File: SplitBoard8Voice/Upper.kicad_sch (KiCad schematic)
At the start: 18 parts, among them J801 A_UPPER, J802 B_UPPER, J803 C_UPPER, J804 D_UPPER, U801 40106, U802 CS5173

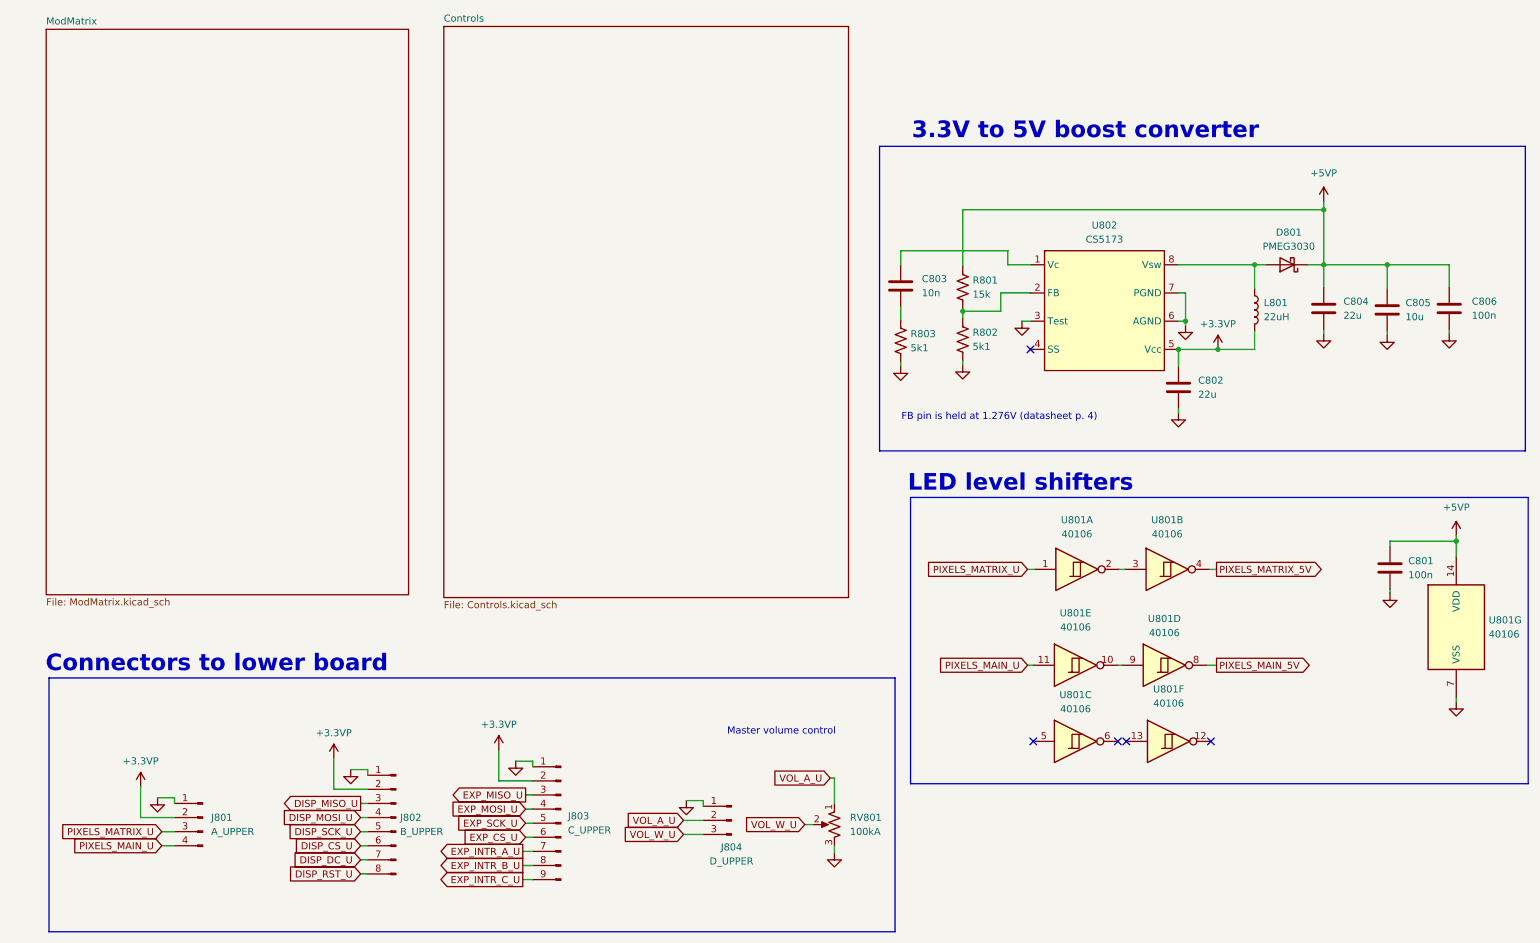
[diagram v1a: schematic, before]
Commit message: back to 3.3v LEDs
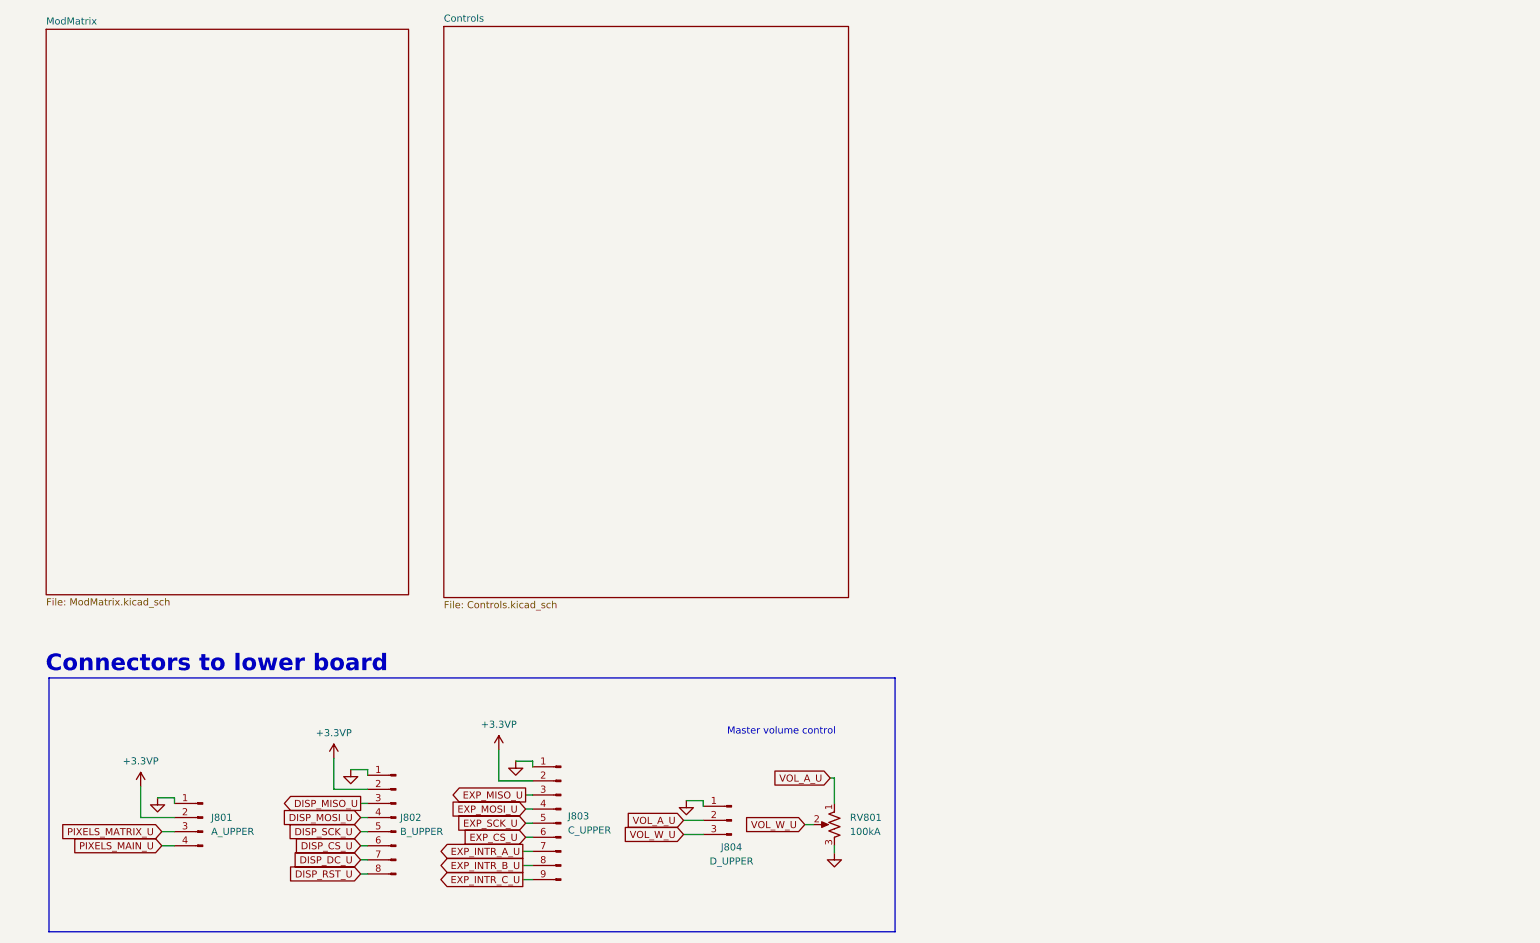
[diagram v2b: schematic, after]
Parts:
- removed C801, C806: 100n, Capacitor_SMD:C_0805_2012Metric, symbol Device:C
- removed C802, C804: 22u, Capacitor_SMD:C_0805_2012Metric, symbol Device:C
- removed C803: 10n, Capacitor_SMD:C_0805_2012Metric, symbol Device:C
- removed C805: 10u, Capacitor_SMD:C_0805_2012Metric, symbol Device:C
- removed D801: PMEG3030, Diode_SMD:D_SOD-123, symbol Device:D_Schottky
- removed L801: 22uH, Inductor_SMD:L_Changjiang_FNR4010S, symbol Device:L
- removed R801: 15k, Resistor_SMD:R_0805_2012Metric, symbol Device:R_US
- removed R802, R803: 5k1, Resistor_SMD:R_0805_2012Metric, symbol Device:R_US
- removed U801: 40106, Package_SO:SOIC-14_3.9x8.7mm_P1.27mm, symbol 4xxx:40106
- removed U802: CS5173, Package_SO:SOIC-8_3.9x4.9mm_P1.27mm, symbol cs5173:CS5173
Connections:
- no-connect marks 5 -> 0
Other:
- note removed: "3.3V to 5V boost converter"
- note removed: "FB pin is held at 1.276V (datasheet p. 4)"
- note removed: "LED level shifters"
